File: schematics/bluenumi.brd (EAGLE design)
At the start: 110 x 60.5 mm, 48 parts, among them IC1 MEGA8-P, J1 POWER_JACKPTH, Q1 16Mhz, Q3 BC337

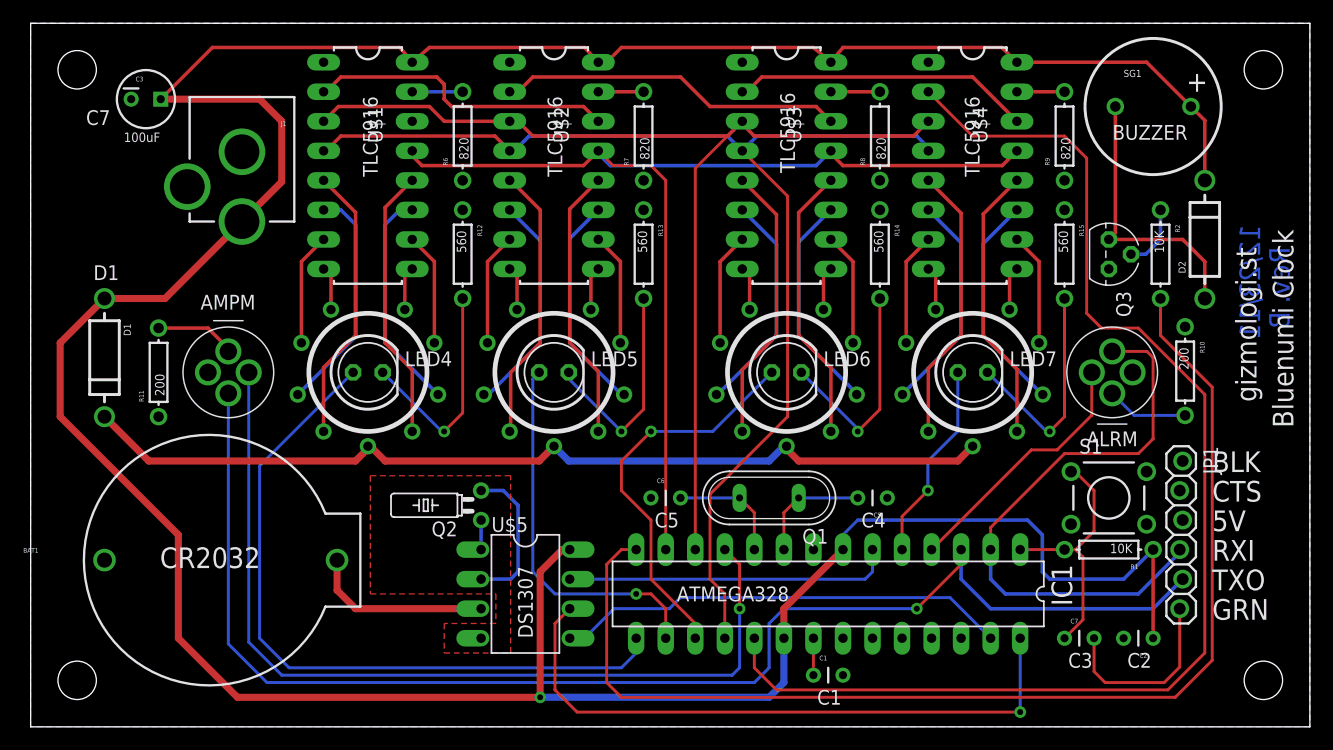
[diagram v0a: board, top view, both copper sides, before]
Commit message: Clean up board layout
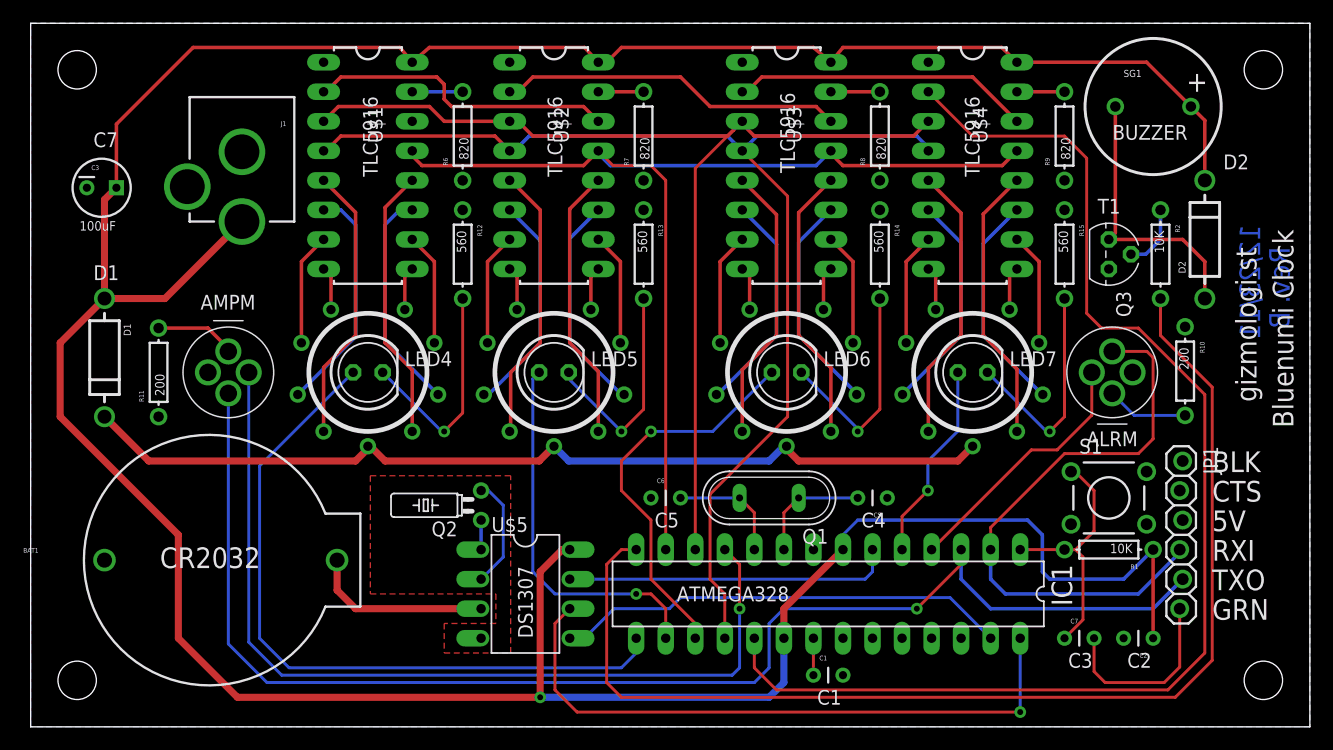
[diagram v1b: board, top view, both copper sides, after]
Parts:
- moved C3 8.52 mm to (6.11, 46.4)
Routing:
- net N$21: track 12.9 -> 9.57 mm
- net VCC: track 296.9 -> 295.8 mm
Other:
- board text added: "D2"
- board text added: "T1"
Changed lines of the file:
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@@
 <text x="67.6275" y="1.905" size="1.27" layer="21" ratio="15">C1</text>
 <text x="94.2975" y="5.08" size="1.27" layer="21" ratio="15">C2</text>
-<text x="4.7625" y="51.7525" size="1.27" layer="21" ratio="15">C7</text>
+<text x="5.3975" y="49.8475" size="1.27" layer="21" ratio="15">C7</text>
 <text x="71.4375" y="17.145" size="1.27" layer="21" ratio="15">C4</text>
 <text x="53.6575" y="17.145" size="1.27" layer="21" ratio="15">C5</text>
@@
 <text x="81.5975" y="47.3075" size="1.27" layer="21" ratio="15" rot="R90">TLC5916</text>
 <text x="5.3975" y="38.4175" size="1.27" layer="21" ratio="15">D1</text>
+<text x="102.5525" y="47.9425" size="1.27" layer="21" ratio="15">D2</text>
+<text x="91.7575" y="44.1325" size="1.27" layer="21" ratio="15">T1</text>
 </plain>
 <attributes>
@@
 <element name="SG1" library="SparkFun" package="BUZZER-12MM-NS" value="BUZZERNS" x="96.52" y="53.34"/>
 <element name="R10" library="SparkFun" package="AXIAL-0.3" value="200" x="99.27" y="30.59" rot="R270"/>
-<element name="C3" library="SparkFun" package="CPOL-RADIAL-10UF-25V" value="100uF" x="9.915" y="53.975"/>
+<element name="C3" library="SparkFun" package="CPOL-RADIAL-10UF-25V" value="100uF" x="6.105" y="46.355"/>
 <element name="R11" library="SparkFun" package="AXIAL-0.3" value="200" x="11" y="30.48" rot="R90"/>
 <element name="LED4" library="led" package="LED5MM" value="" x="29" y="30.48"/>
@@
 <wire x1="83.5025" y1="58.42" x2="84.81" y2="57.15" width="0.3048" layer="1"/>
 <wire x1="18.05" y1="43.45" x2="18.17" y2="43.45" width="0.6096" layer="1"/>
-<wire x1="18.17" y1="43.45" x2="21.59" y2="46.87" width="0.6096" layer="1"/>
 <wire x1="64.77" y1="3.81" x2="64.77" y2="7.62" width="0.6096" layer="16"/>
 <wire x1="63.5" y1="2.54" x2="64.77" y2="3.81" width="0.6096" layer="16"/>
 <wire x1="43.815" y1="2.54" x2="63.5" y2="2.54" width="0.6096" layer="16"/>
-<wire x1="21.59" y1="46.87" x2="21.59" y2="52.07" width="0.6096" layer="1"/>
-<wire x1="21.59" y1="52.07" x2="19.685" y2="53.975" width="0.6096" layer="1"/>
-<wire x1="19.685" y1="53.975" x2="11.185" y2="53.975" width="0.6096" layer="1"/>
-<wire x1="15.63" y1="58.42" x2="31.75" y2="58.42" width="0.3048" layer="1"/>
-<wire x1="11.185" y1="53.975" x2="15.63" y2="58.42" width="0.3048" layer="1"/>
+<wire x1="13.97" y1="58.42" x2="31.75" y2="58.42" width="0.3048" layer="1"/>
 <wire x1="64.77" y1="7.62" x2="64.77" y2="10.16" width="0.6096" layer="1"/>
 <wire x1="64.77" y1="10.16" x2="69.85" y2="15.24" width="0.6096" layer="1"/>
@@
 <wire x1="6.35" y1="36.83" x2="11.55" y2="36.83" width="0.6096" layer="1"/>
 <wire x1="11.55" y1="36.83" x2="18.17" y2="43.45" width="0.6096" layer="1"/>
+<wire x1="7.375" y1="46.355" x2="7.375" y2="51.825" width="0.3048" layer="1"/>
+<wire x1="7.375" y1="51.825" x2="13.97" y2="58.42" width="0.3048" layer="1"/>
+<wire x1="6.35" y1="36.83" x2="6.35" y2="45.33" width="0.6096" layer="1"/>
+<wire x1="6.35" y1="45.33" x2="7.375" y2="46.355" width="0.6096" layer="1"/>
 </signal>
 <signal name="N$9">
@@
 <contactref element="Q2" pad="2"/>
 <contactref element="U$5" pad="2"/>
-<wire x1="38.735" y1="12.7" x2="41.275" y2="12.7" width="0.3048" layer="16"/>
-<wire x1="41.275" y1="12.7" x2="41.91" y2="13.335" width="0.3048" layer="16"/>
-<wire x1="41.91" y1="13.335" x2="41.91" y2="19.05" width="0.3048" layer="16"/>
-<wire x1="41.91" y1="19.05" x2="40.64" y2="20.32" width="0.3048" layer="16"/>
-<wire x1="40.64" y1="20.32" x2="38.735" y2="20.32" width="0.3048" layer="16"/>
+<wire x1="38.735" y1="20.32" x2="39.37" y2="20.32" width="0.254" layer="16"/>
+<wire x1="39.37" y1="20.32" x2="40.64" y2="19.05" width="0.254" layer="16"/>
+<wire x1="40.64" y1="19.05" x2="40.64" y2="14.605" width="0.254" layer="16"/>
+<wire x1="40.64" y1="14.605" x2="38.735" y2="12.7" width="0.254" layer="16"/>
 </signal>
 <signal name="N$34">

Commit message: Create gerber files Update board and schematic so that LED PWM is not on Arduino pins 3 or 11
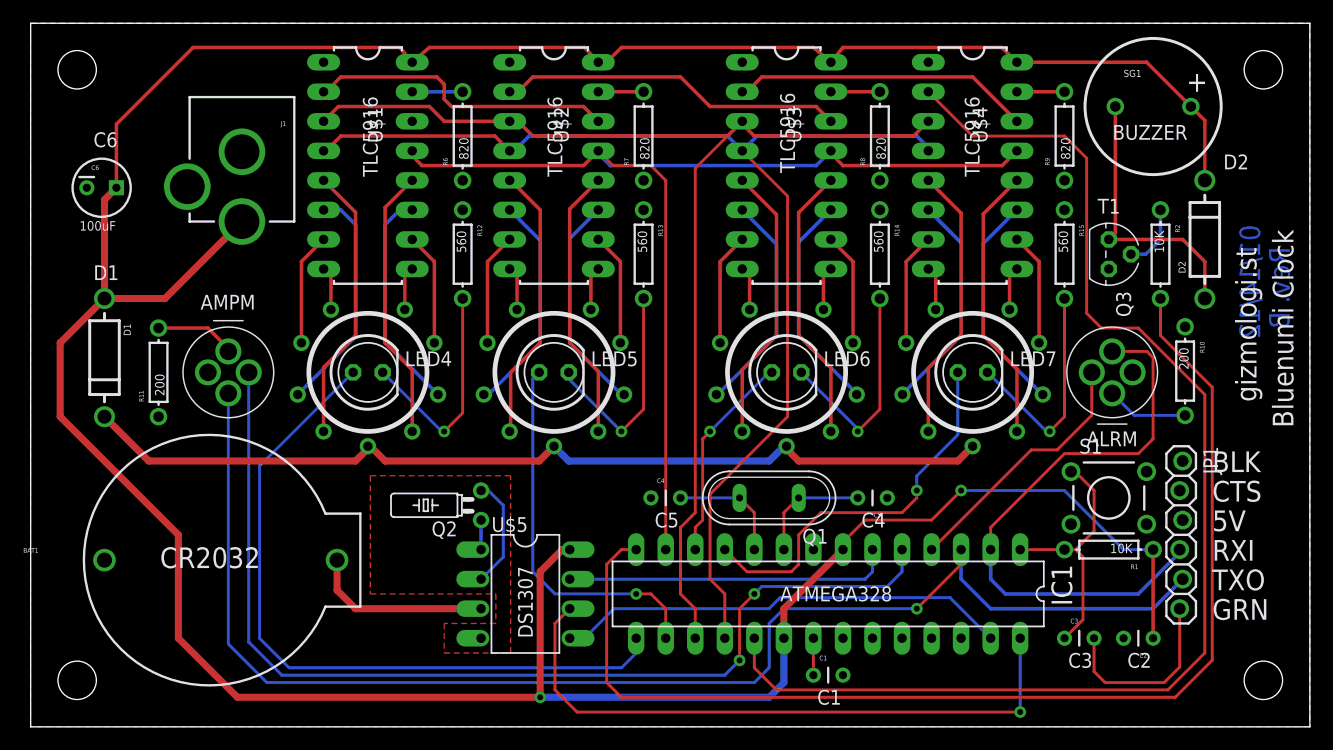
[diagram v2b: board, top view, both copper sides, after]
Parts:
- removed C7: 0.1u, SparkFun:CAP-PTH-SMALL
- added C4: 22p, SparkFun:CAP-PTH-SMALL
- C3: value 100uF -> 0.1u; device SparkFun:CPOL-RADIAL-10UF-25V -> SparkFun:CAP-PTH-SMALL
- C6: value 22p -> 100uF; device SparkFun:CAP-PTH-SMALL -> SparkFun:CPOL-RADIAL-10UF-25V
- moved C3 91.4 mm to (88.9, 7.62)
- moved C6 54.2 mm to (6.11, 46.4)
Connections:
- net CLK: now also IC1.17; no longer IC1.12
- net DTR: now also C3.2; no longer C7.2
- net GND: now also C4.1, C6.2; no longer C3.2, C6.1
- net N$22: now also C4.2; no longer C6.2
- net N$23: now also C3.1; no longer C7.1
- net SECONDS2: now also IC1.12; no longer IC1.17
- net SECONDS3: now also IC1.11; no longer IC1.5
- net SET_ALRM: now also IC1.5; no longer IC1.11
- net VCC: now also C6.1; no longer C3.1
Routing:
- net SECONDS3: track 17.2 -> 33.7 mm
- net SECONDS2: track 34.0 -> 18.1 mm
- net SET_ALRM: track 77.5 -> 88.7 mm, vias 1 -> 2
- net CLK: track 92.7 -> 101.4 mm
- net VCC: track 295.8 -> 293.6 mm, vias 1 -> 2
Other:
- board text added: "01/14/12"
- board text added: "C6"
- board text removed: "12/23/11"
- board text removed: "C7"
